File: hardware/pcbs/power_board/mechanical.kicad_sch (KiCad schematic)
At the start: 7 parts

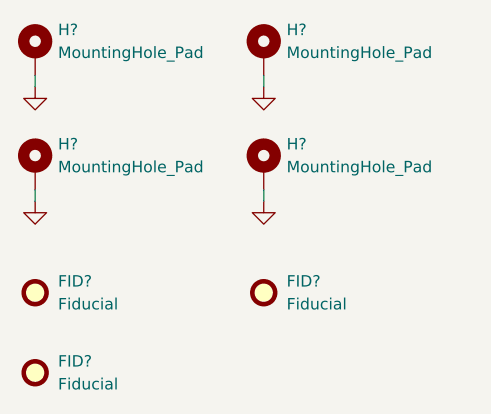
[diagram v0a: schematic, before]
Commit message: power_board: update caps
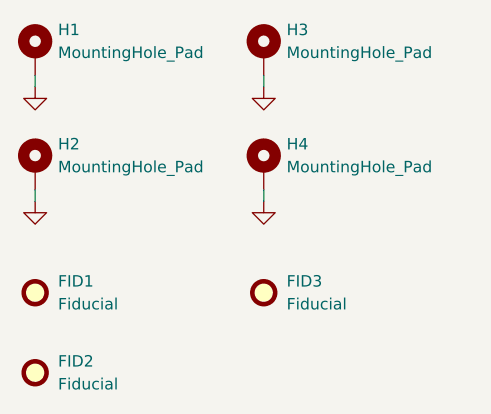
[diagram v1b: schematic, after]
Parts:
- gave numbers to parts that had none: 7
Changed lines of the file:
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@@
   (symbol (lib_id "Mechanical:MountingHole_Pad") (at 90.17 71.12 0) (unit 1)
     (in_bom no) (on_board yes) (dnp no) (fields_autoplaced)
-    (property "Reference" "H?" (at 92.71 68.58 0)
+    (property "Reference" "H2" (at 92.71 68.58 0)
       (effects (font (size 1.27 1.27)) (justify left))
     )
@@
       (project "power_board"
         (path "/4b166175-80a4-48c6-994d-6e62a6160b87/99ad2a2c-266b-4765-b6d1-327c82d6c9e2"
-          (reference "H?") (unit 1)
+          (reference "H2") (unit 1)
         )
       )
@@
   (symbol (lib_id "Mechanical:Fiducial") (at 90.17 85.09 0) (unit 1)
     (in_bom yes) (on_board yes) (dnp no) (fields_autoplaced)
-    (property "Reference" "FID?" (at 92.71 83.82 0)
+    (property "Reference" "FID1" (at 92.71 83.82 0)
       (effects (font (size 1.27 1.27)) (justify left))
     )
@@
       (project "power_board"
         (path "/4b166175-80a4-48c6-994d-6e62a6160b87/99ad2a2c-266b-4765-b6d1-327c82d6c9e2"
-          (reference "FID?") (unit 1)
+          (reference "FID1") (unit 1)
         )
       )
@@
   (symbol (lib_id "Mechanical:Fiducial") (at 90.17 93.98 0) (unit 1)
     (in_bom yes) (on_board yes) (dnp no) (fields_autoplaced)
-    (property "Reference" "FID?" (at 92.71 92.71 0)
+    (property "Reference" "FID2" (at 92.71 92.71 0)
       (effects (font (size 1.27 1.27)) (justify left))
     )
@@
       (project "power_board"
         (path "/4b166175-80a4-48c6-994d-6e62a6160b87/99ad2a2c-266b-4765-b6d1-327c82d6c9e2"
-          (reference "FID?") (unit 1)
+          (reference "FID2") (unit 1)
         )
       )
@@
   (symbol (lib_id "Mechanical:Fiducial") (at 115.57 85.09 0) (unit 1)
     (in_bom yes) (on_board yes) (dnp no) (fields_autoplaced)
-    (property "Reference" "FID?" (at 118.11 83.82 0)
+    (property "Reference" "FID3" (at 118.11 83.82 0)
       (effects (font (size 1.27 1.27)) (justify left))
     )
@@
       (project "power_board"
         (path "/4b166175-80a4-48c6-994d-6e62a6160b87/99ad2a2c-266b-4765-b6d1-327c82d6c9e2"
-          (reference "FID?") (unit 1)
+          (reference "FID3") (unit 1)
         )
       )
@@
   (symbol (lib_id "Mechanical:MountingHole_Pad") (at 115.57 58.42 0) (unit 1)
     (in_bom no) (on_board yes) (dnp no) (fields_autoplaced)
-    (property "Reference" "H?" (at 118.11 55.88 0)
+    (property "Reference" "H3" (at 118.11 55.88 0)
       (effects (font (size 1.27 1.27)) (justify left))
     )
@@
       (project "power_board"
         (path "/4b166175-80a4-48c6-994d-6e62a6160b87/99ad2a2c-266b-4765-b6d1-327c82d6c9e2"
-          (reference "H?") (unit 1)
+          (reference "H3") (unit 1)
         )
       )
@@
   (symbol (lib_id "power:GND") (at 90.17 62.23 0) (unit 1)
     (in_bom yes) (on_board yes) (dnp no) (fields_autoplaced)
-    (property "Reference" "#PWR0106" (at 90.17 68.58 0)
+    (property "Reference" "#PWR077" (at 90.17 68.58 0)
       (effects (font (size 1.27 1.27)) hide)
     )
@@
       (project "power_board"
         (path "/4b166175-80a4-48c6-994d-6e62a6160b87/99ad2a2c-266b-4765-b6d1-327c82d6c9e2"
-          (reference "#PWR0106") (unit 1)
+          (reference "#PWR077") (unit 1)
         )
       )
@@
   (symbol (lib_id "Mechanical:MountingHole_Pad") (at 115.57 71.12 0) (unit 1)
     (in_bom no) (on_board yes) (dnp no) (fields_autoplaced)
-    (property "Reference" "H?" (at 118.11 68.58 0)
+    (property "Reference" "H4" (at 118.11 68.58 0)
       (effects (font (size 1.27 1.27)) (justify left))
     )
@@
       (project "power_board"
         (path "/4b166175-80a4-48c6-994d-6e62a6160b87/99ad2a2c-266b-4765-b6d1-327c82d6c9e2"
-          (reference "H?") (unit 1)
+          (reference "H4") (unit 1)
         )
       )
@@
   (symbol (lib_id "power:GND") (at 115.57 62.23 0) (unit 1)
     (in_bom yes) (on_board yes) (dnp no) (fields_autoplaced)
-    (property "Reference" "#PWR0107" (at 115.57 68.58 0)
+    (property "Reference" "#PWR079" (at 115.57 68.58 0)
       (effects (font (size 1.27 1.27)) hide)
     )
@@
       (project "power_board"
         (path "/4b166175-80a4-48c6-994d-6e62a6160b87/99ad2a2c-266b-4765-b6d1-327c82d6c9e2"
-          (reference "#PWR0107") (unit 1)
+          (reference "#PWR079") (unit 1)
         )
       )
@@
   (symbol (lib_id "Mechanical:MountingHole_Pad") (at 90.17 58.42 0) (unit 1)
     (in_bom no) (on_board yes) (dnp no) (fields_autoplaced)
-    (property "Reference" "H?" (at 92.71 55.88 0)
+    (property "Reference" "H1" (at 92.71 55.88 0)
       (effects (font (size 1.27 1.27)) (justify left))
     )
@@
       (project "power_board"
         (path "/4b166175-80a4-48c6-994d-6e62a6160b87/99ad2a2c-266b-4765-b6d1-327c82d6c9e2"
-          (reference "H?") (unit 1)
+          (reference "H1") (unit 1)
         )
       )
@@
   (symbol (lib_id "power:GND") (at 115.57 74.93 0) (unit 1)
     (in_bom yes) (on_board yes) (dnp no) (fields_autoplaced)
-    (property "Reference" "#PWR0109" (at 115.57 81.28 0)
+    (property "Reference" "#PWR080" (at 115.57 81.28 0)
       (effects (font (size 1.27 1.27)) hide)
     )
@@
       (project "power_board"
         (path "/4b166175-80a4-48c6-994d-6e62a6160b87/99ad2a2c-266b-4765-b6d1-327c82d6c9e2"
-          (reference "#PWR0109") (unit 1)
+          (reference "#PWR080") (unit 1)
         )
       )
@@
   (symbol (lib_id "power:GND") (at 90.17 74.93 0) (unit 1)
     (in_bom yes) (on_board yes) (dnp no) (fields_autoplaced)
-    (property "Reference" "#PWR0108" (at 90.17 81.28 0)
+    (property "Reference" "#PWR078" (at 90.17 81.28 0)
       (effects (font (size 1.27 1.27)) hide)
     )
@@
       (project "power_board"
         (path "/4b166175-80a4-48c6-994d-6e62a6160b87/99ad2a2c-266b-4765-b6d1-327c82d6c9e2"
-          (reference "#PWR0108") (unit 1)
-        )
-      )
+          (reference "#PWR078") (unit 1)
+        )
+      )

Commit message: audio_board, power_board: update shop and part links
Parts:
- FID1, FID2, FID3: now left out of the parts list
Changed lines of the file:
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@@
 		(unit 1)
 		(exclude_from_sim no)
-		(in_bom yes)
+		(in_bom no)
 		(on_board yes)
 		(dnp no)
@@
 		(unit 1)
 		(exclude_from_sim no)
-		(in_bom yes)
+		(in_bom no)
 		(on_board yes)
 		(dnp no)
@@
 		(unit 1)
 		(exclude_from_sim no)
-		(in_bom yes)
+		(in_bom no)
 		(on_board yes)
 		(dnp no)

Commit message: power_board: holes with larger keepouts
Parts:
- H1, H2, H3, H4: footprint MountingHole:MountingHole_3.2mm_M3_DIN965_Pad -> conn:MountingHole_3.2mm_M3_keepout
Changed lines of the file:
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@@
 			)
 		)
-		(property "Footprint" "MountingHole:MountingHole_3.2mm_M3_DIN965_Pad"
+		(property "Footprint" "conn:MountingHole_3.2mm_M3_keepout"
 			(at 90.17 71.12 0)
 			(effects
@@
 			)
 		)
-		(property "Footprint" "MountingHole:MountingHole_3.2mm_M3_DIN965_Pad"
+		(property "Footprint" "conn:MountingHole_3.2mm_M3_keepout"
 			(at 115.57 58.42 0)
 			(effects
@@
 			)
 		)
-		(property "Footprint" "MountingHole:MountingHole_3.2mm_M3_DIN965_Pad"
+		(property "Footprint" "conn:MountingHole_3.2mm_M3_keepout"
 			(at 115.57 71.12 0)
 			(effects
@@
 			)
 		)
-		(property "Footprint" "MountingHole:MountingHole_3.2mm_M3_DIN965_Pad"
+		(property "Footprint" "conn:MountingHole_3.2mm_M3_keepout"
 			(at 90.17 58.42 0)
 			(effects
